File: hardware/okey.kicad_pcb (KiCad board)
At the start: 2 copper layers, 263.4 x 349.9 mm, 160 parts, among them IC1 4094N, IC2 4094N, J1 RJ45, J2 RJ45, P1 ROW_JMP, P10 CONN_02X06, P11 CONN_02X06, P12 CONN_02X06, P13 CONN_02X06, P14 CONN_02X06, P15 CONN_02X06, P16 CONN_02X08, P17 CONN_01X01, P18 CONN_02X08, P19 CONN_01X01, P2 CONN_02X13, P20 CONN_01X01, P21 CONN_01X01, P22 CONN_02X08, P23 CONN_02X08, P24 CONN_02X06, P25 CONN_02X06, P26 CONN_02X06, P27 CONN_02X06, P28 CONN_02X06, P29 CONN_02X06, P3 CONN_02X03, P30 CONN_02X08, P31 CONN_02X03, P32 CONN_02X03, P33 CONN_02X06, P34 CONN_02X06, P35 CONN_02X06, P36 CONN_02X06, P37 CONN_02X06, P38 CONN_02X06, P39 CONN_01X01, P4 CONN_02X08, P40 CONN_02X03, P41 CONN_02X06, P42 CONN_02X06, P43 CONN_02X06, P44 CONN_02X06, P45 CONN_02X06, P46 CONN_02X06, P47 CONN_01X01, P48 CONN_02X03, P5 CONN_02X03, P6 CONN_02X10, P7 CONN_02X03, P8 CONN_01X01, P9 CONN_02X08, Q1 Q_NPN_BCE, Q2 Q_NPN_BCE, Q3 Q_NPN_BCE, SW1 MX_D, SW10 MX_D, SW11 MX_D, SW12 MX_D, SW13 MX_D, SW14 MX_D, SW15 MX_D, SW16 MX_D, SW17 MX_D, SW18 MX_D, SW19 SW_PUSH, SW2 MX_D, SW20 SW_PUSH, SW21 SW_PUSH, SW22 SW_PUSH, SW23 SW_PUSH, SW24 SW_PUSH, SW25 SW_PUSH, SW26 SW_PUSH, SW27 SW_PUSH, SW28 SW_PUSH, SW29 SW_PUSH, SW3 MX_D, SW30 SW_PUSH, SW31 SW_PUSH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

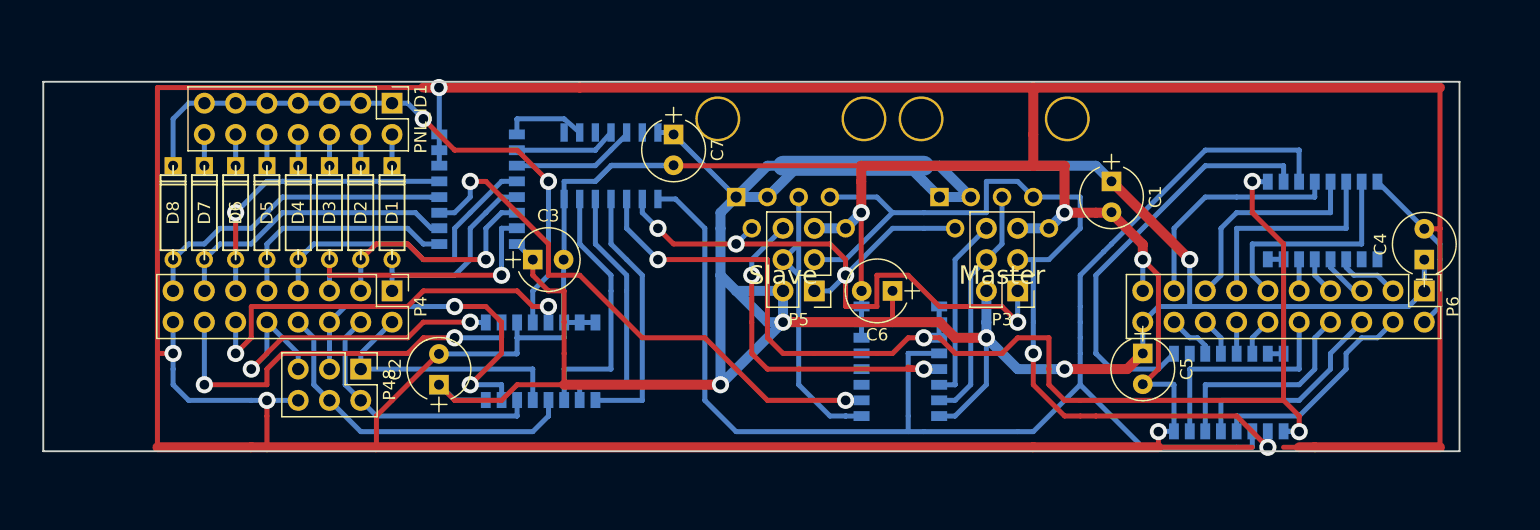
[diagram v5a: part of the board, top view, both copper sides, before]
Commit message: squash! ... hardware: rework SPI board as SMD board with smaller dimensions.
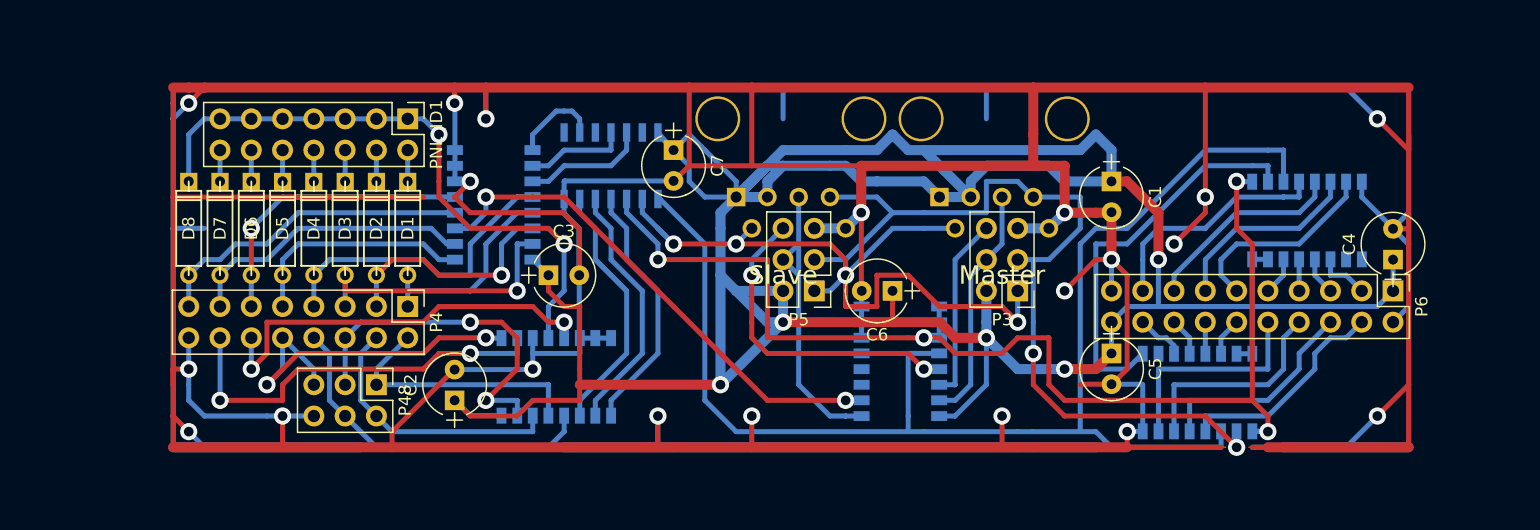
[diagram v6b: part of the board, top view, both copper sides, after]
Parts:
- moved C4 2.54 mm to (129.5, 40.6)
- moved P6 2.54 mm to (129.5, 43.2)
- moved C5 2.54 mm to (106.7, 48.3)
- moved IC1 2.54 mm to (113.7, 51.4)
- moved C2 1.80 mm to (53.3, 52.1)
- moved D1 1.80 mm to (49.5, 38.1)
- moved D2 1.80 mm to (47.0, 38.1)
- moved D3 1.80 mm to (44.5, 38.1)
- moved MUX_COL1 1.80 mm to (56.5, 36.2)
- moved P4 1.80 mm to (49.5, 44.5)
- moved D8 1.80 mm to (31.8, 38.1)
- moved PNL_ID1 1.80 mm to (49.5, 29.2)
- moved C3 1.80 mm to (61.0, 41.9)
- moved D4 1.80 mm to (41.9, 38.1)
- moved D5 1.80 mm to (39.4, 38.1)
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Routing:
- net GND: track 456.7 -> 859.8 mm, vias 8 -> 20
- net VDD: track 245.5 -> 285.8 mm
- net Net-(IC1-Pad1): track 99.0 -> 94.9 mm
- net Net-(J2-Pad4): track 29.7 -> 26.2 mm
- net Net-(MUX_COL1-Pad3): track 44.9 -> 41.7 mm
- net Net-(MUX_ROW1-Pad11): track 21.2 -> 24.3 mm
- net Net-(MUX_ROW1-Pad9): track 21.2 -> 24.4 mm
- net Net-(IC1-Pad2): track 73.1 -> 70.6 mm
- net Net-(IC1-Pad3): track 112.2 -> 109.8 mm
- net /Panel Generic SPI01/reset: track 59.0 -> 60.8 mm
- net Net-(IC2-Pad6): track 17.8 -> 16.1 mm
- net Net-(IC2-Pad7): track 18.3 -> 16.6 mm
- net Net-(IC1-Pad9): track 34.0 -> 32.4 mm
- net Net-(IC2-Pad5): track 17.5 -> 16.6 mm
- net Net-(IC2-Pad11): track 5.26 -> 4.35 mm
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- added copper zone on B.Cu, net GND
- added copper zone on F.Cu, net GND
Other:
- outline, holes or cut-outs redrawn

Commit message: hardware: misc minor SPI board cleanup
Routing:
- net GND: track 859.8 -> 968.6 mm, vias 20 -> 21
- net Net-(IC1-Pad1): track 94.9 -> 90.6 mm
- net Net-(IC1-Pad2): track 70.6 -> 74.4 mm
- net Net-(MUX_ROW1-Pad2): track 32.8 -> 30.6 mm
- net Net-(IC1-Pad7): track 17.7 -> 15.5 mm
- net Net-(MUX_ROW1-Pad1): track 29.9 -> 31.9 mm
- net Net-(IC1-Pad6): track 17.5 -> 16.1 mm
- net VDD: track 285.8 -> 284.7 mm, vias 5 -> 4
- net /Panel Generic SPI01/reset: track 60.8 -> 60.0 mm
- net Net-(IC1-Pad5): track 17.3 -> 16.6 mm
- net Net-(IC1-Pad3): track 109.8 -> 110.3 mm
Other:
- board text added: "4024"
- board text added: "4051"
- board text added: "4053"
- board text added: "4094"
- board text added: "alt C1"

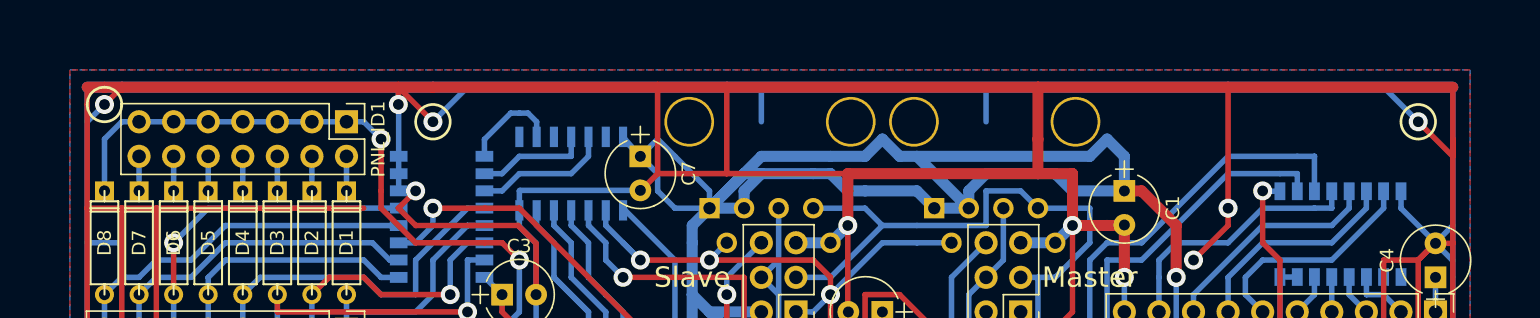
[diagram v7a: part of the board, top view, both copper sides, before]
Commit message: hardware, SPI-board: RJ45-jack shielding
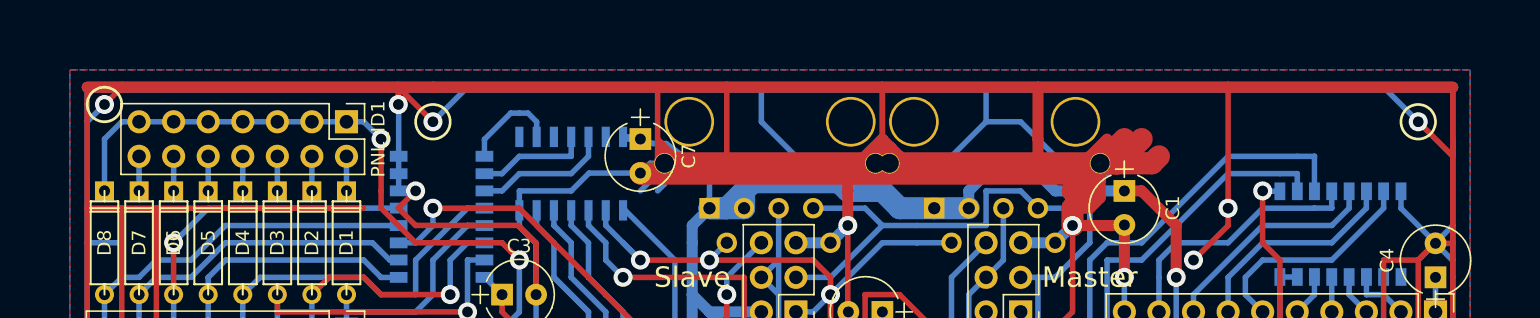
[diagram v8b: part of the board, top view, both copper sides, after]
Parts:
- J1, J2: footprint Connect:RJ45_8 -> custom_footprints:RJ45_8G
- moved C7 1.27 mm to (71.1, 30.5)
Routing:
- net GND: track 968.6 -> 1140.4 mm
- net VDD: track 284.7 -> 231.5 mm
